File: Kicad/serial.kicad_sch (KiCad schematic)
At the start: 9 parts, among them J13001 Conn_02x05, J13002 DB9_Male_MountingHoles, U13001 ST3232CDR

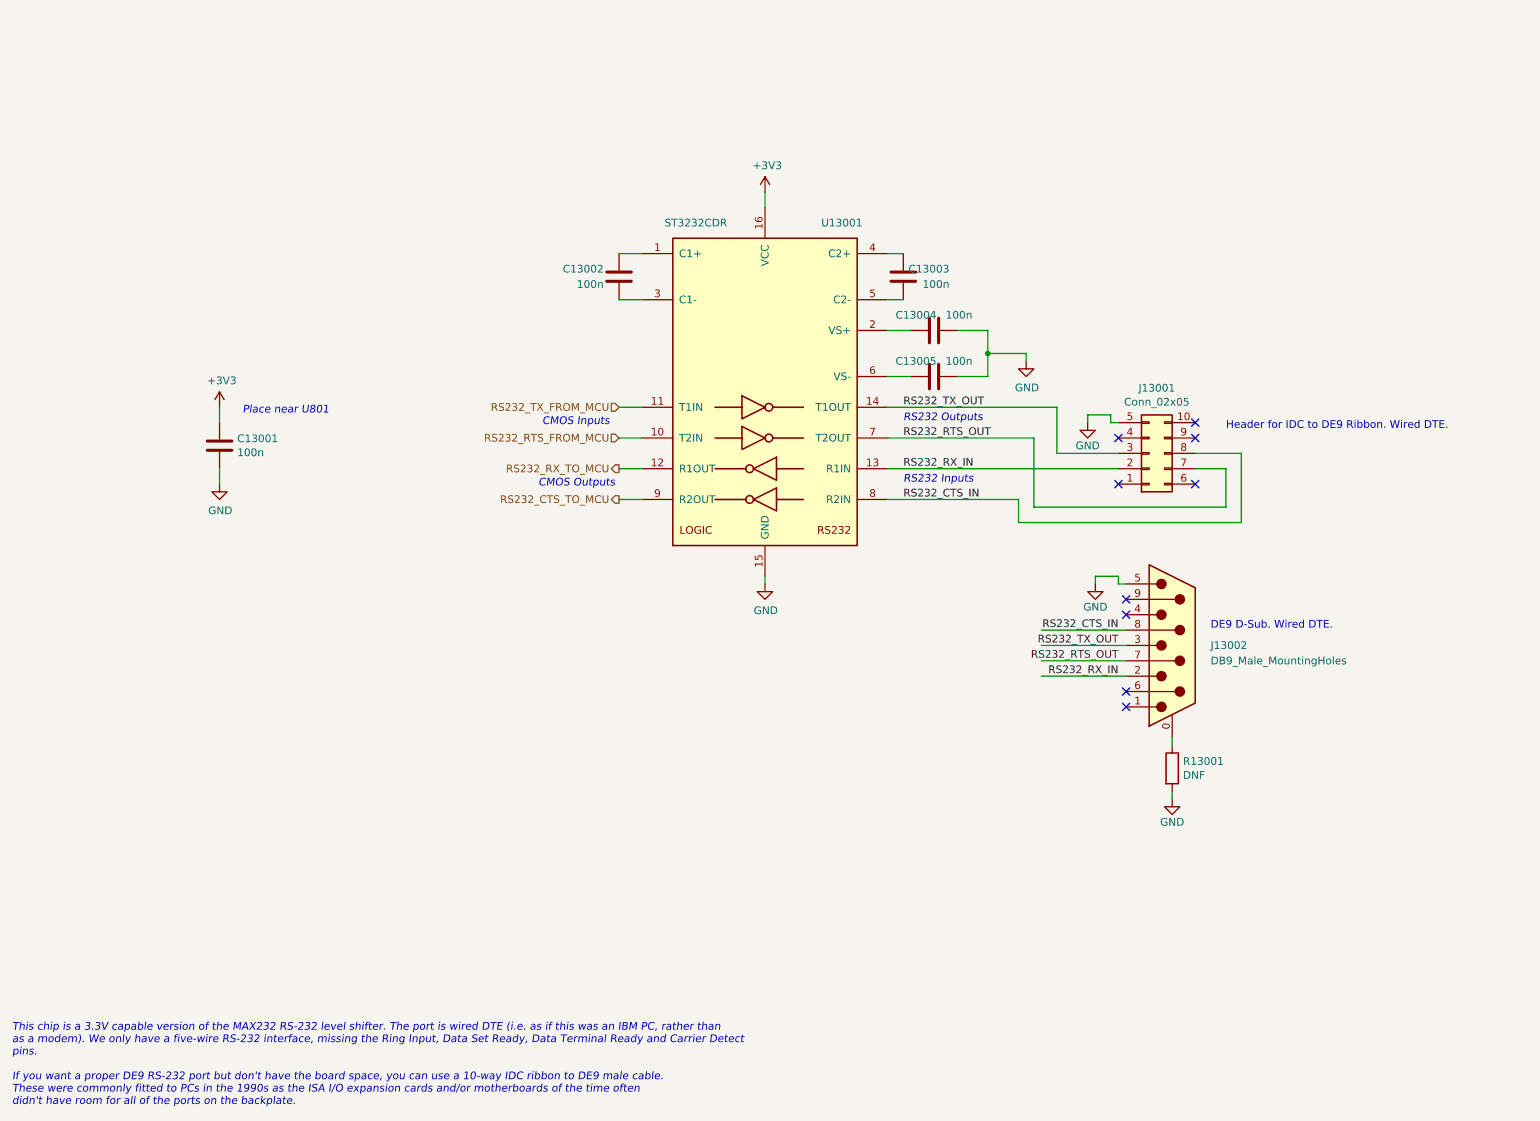
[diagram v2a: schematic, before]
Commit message: Re-imported from Neotron Pico v1.1.
This time I deleted the sheets from the top level and then re-added pointing at the new files. I also reset the PCB dimensions to match the Neotron Pico.

This seems to have done a better job importing footprints.
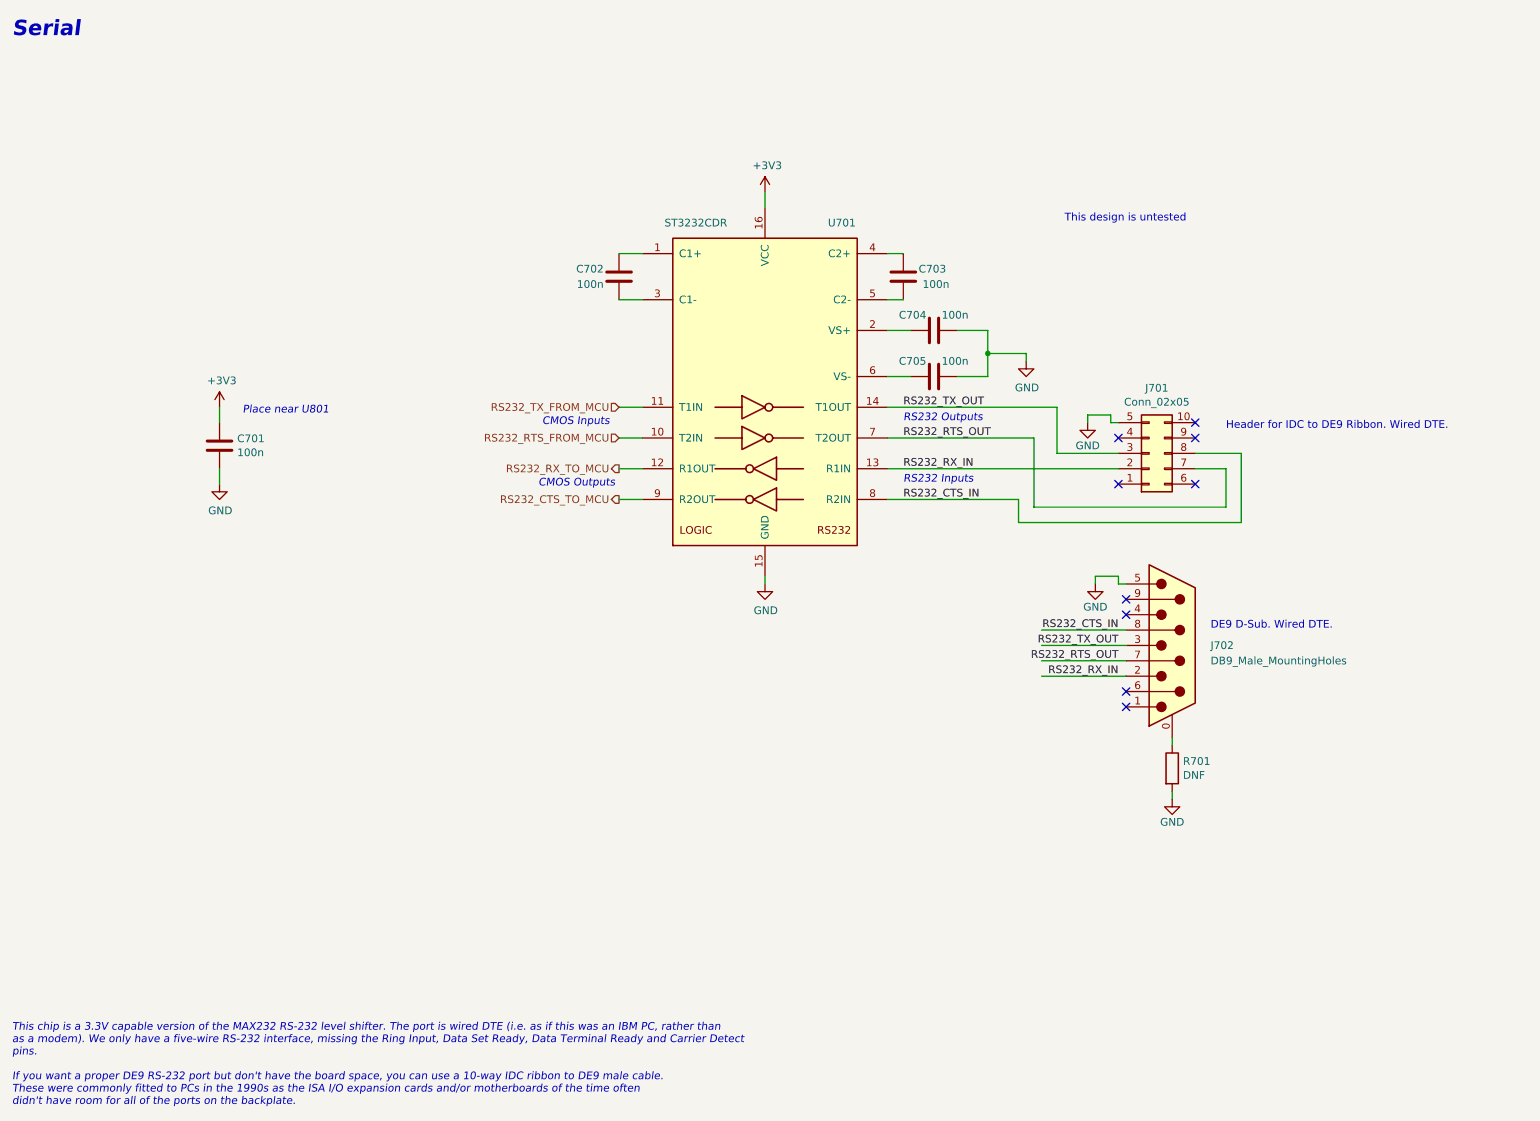
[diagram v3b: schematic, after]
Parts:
- renumbered C13001 to C701, C13002 to C702, C13003 to C703, C13004 to C704, C13005 to C705, J13001 to J701, J13002 to J702, R13001 to R701, U13001 to U701
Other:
- note added: "Serial"
- note added: "This design is untested"
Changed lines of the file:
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@@
     (company "https://neotron-compute.github.io/")
     (comment 1 "Licenced as CC BY-SA")
-    (comment 2 "Copyright (c) The Neotron Developers, 2021")
+    (comment 2 "Copyright (c) The Neotron Developers, 2022")
   )
   (junction (at 175.26 71.12) (diameter 0) (color 0 0 0 0)
@@
     (effects (font (size 1.27 1.27) italic) (justify left bottom))
   )
+  (text "Serial" (at 13.97 19.05 0)
+    (effects (font (size 2.54 2.54) (thickness 0.508) bold italic) (justify left bottom))
+  )
+  (text "This design is untested" (at 187.96 49.53 0)
+    (effects (font (size 1.27 1.27)) (justify left bottom))
+  )
   (text "Place near U801" (at 52.07 81.28 0)
     (effects (font (size 1.27 1.27) italic) (justify left bottom))
@@
   (symbol (lib_id "Connector_Generic:Conn_02x05_Top_Bottom") (at 201.93 87.63 0) (mirror x) (unit 1)
     (in_bom yes) (on_board yes)
-    (property "Reference" "J13001" (id 0) (at 203.2 76.835 0))
+    (property "Reference" "J701" (id 0) (at 203.2 76.835 0))
     (property "Value" "Conn_02x05" (id 1) (at 203.2 79.1464 0))
     (property "Footprint" "Connector_IDC:IDC-Header_2x05_P2.54mm_Vertical" (id 2) (at 201.93 87.63 0)
@@
   (symbol (lib_id "power:GND") (at 191.77 82.55 0) (unit 1)
     (in_bom yes) (on_board yes)
-    (property "Reference" "#PWR013006" (id 0) (at 191.77 88.9 0)
+    (property "Reference" "#PWR0706" (id 0) (at 191.77 88.9 0)
       (effects (font (size 1.27 1.27)) hide)
     )
@@
   (symbol (lib_id "Interface_UART:MAX232") (at 138.43 77.47 0) (unit 1)
     (in_bom yes) (on_board yes)
-    (property "Reference" "U13001" (id 0) (at 151.13 49.53 0))
+    (property "Reference" "U701" (id 0) (at 151.13 49.53 0))
     (property "Value" "ST3232CDR" (id 1) (at 127 49.53 0))
     (property "Footprint" "Package_SO:SO-16_5.3x10.2mm_P1.27mm" (id 2) (at 139.7 104.14 0)
@@
   (symbol (lib_id "power:GND") (at 181.61 72.39 0) (unit 1)
     (in_bom yes) (on_board yes)
-    (property "Reference" "#PWR013005" (id 0) (at 181.61 78.74 0)
+    (property "Reference" "#PWR0705" (id 0) (at 181.61 78.74 0)
       (effects (font (size 1.27 1.27)) hide)
     )
@@
   (symbol (lib_id "Device:C") (at 161.29 58.42 0) (unit 1)
     (in_bom yes) (on_board yes)
-    (property "Reference" "C13003" (id 0) (at 168.91 57.15 0)
-      (effects (font (size 1.27 1.27)) (justify right))
+    (property "Reference" "C703" (id 0) (at 163.83 57.15 0)
+      (effects (font (size 1.27 1.27)) (justify left))
     )
     (property "Value" "100n" (id 1) (at 168.91 59.69 0)
@@
   (symbol (lib_id "Device:C") (at 166.37 74.93 270) (unit 1)
     (in_bom yes) (on_board yes)
-    (property "Reference" "C13005" (id 0) (at 160.02 72.39 90)
-      (effects (font (size 1.27 1.27)) (justify left))
-    )
-    (property "Value" "100n" (id 1) (at 172.72 72.39 90)
+    (property "Reference" "C705" (id 0) (at 165.1 72.39 90)
       (effects (font (size 1.27 1.27)) (justify right))
     )
+    (property "Value" "100n" (id 1) (at 167.64 72.39 90)
+      (effects (font (size 1.27 1.27)) (justify left))
+    )
     (property "Footprint" "Capacitor_SMD:C_0805_2012Metric_Pad1.18x1.45mm_HandSolder" (id 2) (at 162.56 75.8952 0)
       (effects (font (size 1.27 1.27)) hide)
@@
   (symbol (lib_id "Device:C") (at 114.3 58.42 180) (unit 1)
     (in_bom yes) (on_board yes)
-    (property "Reference" "C13002" (id 0) (at 111.76 57.15 0)
+    (property "Reference" "C702" (id 0) (at 111.76 57.15 0)
       (effects (font (size 1.27 1.27)) (justify left))
     )
@@
   (symbol (lib_id "Device:C") (at 48.26 86.36 180) (unit 1)
     (in_bom yes) (on_board yes)
-    (property "Reference" "C13001" (id 0) (at 51.181 85.1916 0)
+    (property "Reference" "C701" (id 0) (at 51.181 85.1916 0)
       (effects (font (size 1.27 1.27)) (justify right))
     )
@@
   (symbol (lib_id "power:+3V3") (at 138.43 44.45 0) (unit 1)
     (in_bom yes) (on_board yes)
-    (property "Reference" "#PWR013003" (id 0) (at 138.43 48.26 0)
+    (property "Reference" "#PWR0703" (id 0) (at 138.43 48.26 0)
       (effects (font (size 1.27 1.27)) hide)
     )
@@
   (symbol (lib_id "power:+3V3") (at 48.26 80.01 0) (unit 1)
     (in_bom yes) (on_board yes)
-    (property "Reference" "#PWR013001" (id 0) (at 48.26 83.82 0)
+    (property "Reference" "#PWR0701" (id 0) (at 48.26 83.82 0)
       (effects (font (size 1.27 1.27)) hide)
     )
@@
   (symbol (lib_id "power:GND") (at 48.26 92.71 0) (unit 1)
     (in_bom yes) (on_board yes)
-    (property "Reference" "#PWR013002" (id 0) (at 48.26 99.06 0)
+    (property "Reference" "#PWR0702" (id 0) (at 48.26 99.06 0)
       (effects (font (size 1.27 1.27)) hide)
     )
@@
   (symbol (lib_id "Device:C") (at 166.37 67.31 270) (unit 1)
     (in_bom yes) (on_board yes)
-    (property "Reference" "C13004" (id 0) (at 160.02 64.77 90)
-      (effects (font (size 1.27 1.27)) (justify left))
-    )
-    (property "Value" "100n" (id 1) (at 172.72 64.77 90)
+    (property "Reference" "C704" (id 0) (at 165.1 64.77 90)
       (effects (font (size 1.27 1.27)) (justify right))
     )
+    (property "Value" "100n" (id 1) (at 167.64 64.77 90)
+      (effects (font (size 1.27 1.27)) (justify left))
+    )
     (property "Footprint" "Capacitor_SMD:C_0805_2012Metric_Pad1.18x1.45mm_HandSolder" (id 2) (at 162.56 68.2752 0)
       (effects (font (size 1.27 1.27)) hide)
@@
   (symbol (lib_id "power:GND") (at 138.43 109.22 0) (unit 1)
     (in_bom yes) (on_board yes)
-    (property "Reference" "#PWR013004" (id 0) (at 138.43 115.57 0)
+    (property "Reference" "#PWR0704" (id 0) (at 138.43 115.57 0)
       (effects (font (size 1.27 1.27)) hide)
     )
@@
   (symbol (lib_id "Connector:DB9_Male_MountingHoles") (at 205.74 119.38 0) (unit 1)
     (in_bom yes) (on_board yes)
-    (property "Reference" "J13002" (id 0) (at 212.09 119.38 0)
+    (property "Reference" "J702" (id 0) (at 212.09 119.38 0)
       (effects (font (size 1.27 1.27)) (justify left))
     )
@@
   (symbol (lib_id "power:GND") (at 193.04 109.22 0) (unit 1)
     (in_bom yes) (on_board yes)
-    (property "Reference" "#PWR013007" (id 0) (at 193.04 115.57 0)
+    (property "Reference" "#PWR0707" (id 0) (at 193.04 115.57 0)
       (effects (font (size 1.27 1.27)) hide)
     )
@@
   (symbol (lib_id "power:GND") (at 205.74 144.78 0) (unit 1)
     (in_bom yes) (on_board yes)
-    (property "Reference" "#PWR013008" (id 0) (at 205.74 151.13 0)
+    (property "Reference" "#PWR0708" (id 0) (at 205.74 151.13 0)
       (effects (font (size 1.27 1.27)) hide)
     )
@@
   (symbol (lib_id "Device:R") (at 205.74 139.7 0) (unit 1)
     (in_bom yes) (on_board yes)
-    (property "Reference" "R13001" (id 0) (at 207.518 138.5316 0)
-      (effects (font (size 1.27 1.27)) (justify left))
-    )
+    (property "Reference" "R701" (id 0) (at 207.518 138.5316 0)
+      (effects (font (size 1.27 1.27)) (justify left))
+    )
